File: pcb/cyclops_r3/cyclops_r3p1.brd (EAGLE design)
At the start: 69.8 x 53.3 mm, 55 parts, among them Q1 SUM11006, Q2 IRF510, U1 MCP4921, U2 317-N, U3 ADR03, U4 OP1177, U5 LM324N, U6 ZXTD45

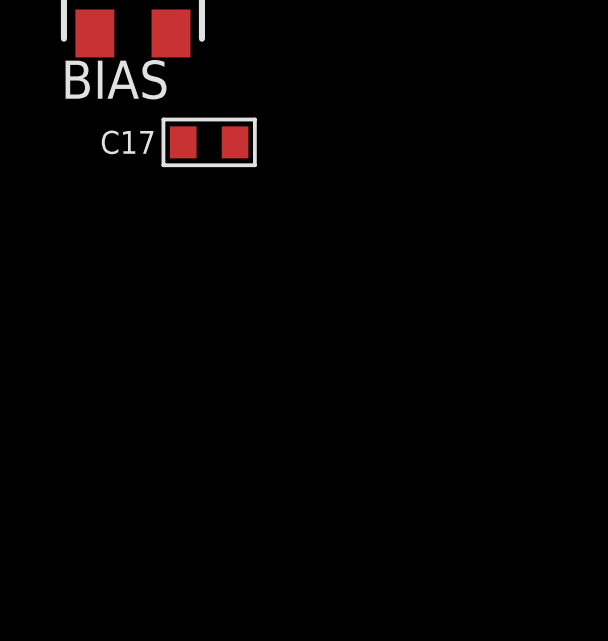
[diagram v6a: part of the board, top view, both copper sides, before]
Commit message: Added some test points to the the circuit and a design note.
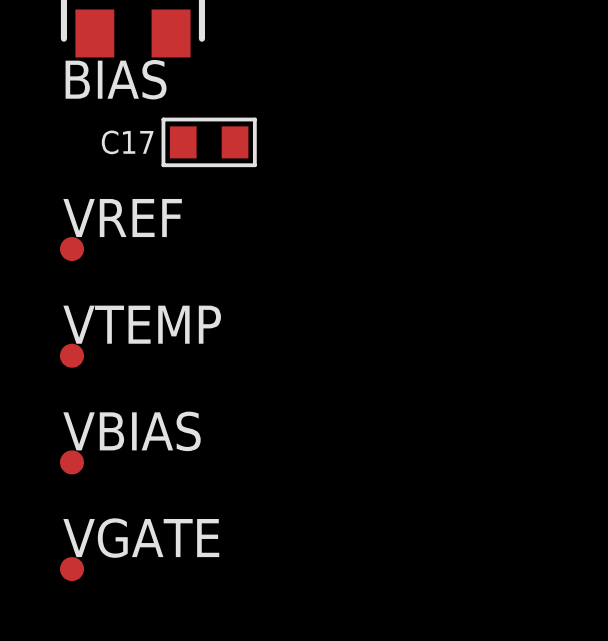
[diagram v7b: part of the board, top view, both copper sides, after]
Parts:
- added VBIAS, VGATE, VREF, VTEMP: TPTP08R, cyclops:TP08R
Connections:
- net REFA2X renamed VREF2X
- removed net REFA: C2.1, REF_ADJ.1, U1.6, U3.4, U5.12
- net N$13: now also VGATE.TP
- net N$4: now also VBIAS.TP
- net VREF: now also C2.1, REF_ADJ.1, U1.6, U3.4, U5.12, VREF.TP
- net VTEMP: now also VTEMP.TP
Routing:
- net VREF: track 40.7 -> 118.9 mm
- net REFA: track 78.2 -> 0.00 mm
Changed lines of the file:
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@@
 <element name="BIAS" library="cyclops" package="SM-42/43W" value="10k" x="-1.524" y="-13.716"/>
 <element name="C17" library="cyclops" package="0603" value=".1uF" x="1.016" y="-18.796"/>
+<element name="VREF" library="cyclops" package="TP08R" value="TPTP08R" x="-3.556" y="-22.352">
+<attribute name="TP_SIGNAL_NAME" value="" x="-3.556" y="-22.352" size="1.778" layer="27" display="off"/>
+</element>
+<element name="VTEMP" library="cyclops" package="TP08R" value="TPTP08R" x="-3.556" y="-25.908">
+<attribute name="TP_SIGNAL_NAME" value="" x="-3.556" y="-25.908" size="1.778" layer="27" display="off"/>
+</element>
+<element name="VBIAS" library="cyclops" package="TP08R" value="TPTP08R" x="-3.556" y="-29.464">
+<attribute name="TP_SIGNAL_NAME" value="" x="-3.556" y="-29.464" size="1.778" layer="27" display="off"/>
+</element>
+<element name="VGATE" library="cyclops" package="TP08R" value="TPTP08R" x="-3.556" y="-33.02">
+<attribute name="TP_SIGNAL_NAME" value="" x="-3.556" y="-33.02" size="1.778" layer="27" display="off"/>
+</element>
 </elements>
 <signals>
@@
 <wire x1="58.438" y1="39.116" x2="59.69" y2="39.116" width="0.254" layer="1"/>
 </signal>
-<signal name="REFA">
-<contactref element="U1" pad="6"/>
-<contactref element="C2" pad="1"/>
-<contactref element="U3" pad="4"/>
-<contactref element="REF_ADJ" pad="1"/>
-<wire x1="42.09" y1="28.9538" x2="42.09" y2="30.988" width="0.8128" layer="1"/>
-<wire x1="42.09" y1="30.988" x2="42.09" y2="31.168" width="0.8128" layer="1"/>
-<wire x1="42.09" y1="31.168" x2="42.164" y2="31.242" width="0.8128" layer="1"/>
-<wire x1="52.204078125" y1="31.242" x2="53.34" y2="32.377921875" width="0.8128" layer="1"/>
-<wire x1="53.34" y1="32.377921875" x2="53.34" y2="34.5186" width="0.8128" layer="1"/>
-<wire x1="53.34" y1="34.5186" x2="53.3654" y2="34.544" width="0.8128" layer="1"/>
-<wire x1="53.3654" y1="34.544" x2="53.3654" y2="34.5694" width="0.8128" layer="1"/>
-<wire x1="53.3654" y1="34.5694" x2="54.229" y2="35.433" width="0.6096" layer="1"/>
-<wire x1="54.229" y1="35.433" x2="56.328" y2="35.433" width="0.6096" layer="1"/>
-<wire x1="7.782" y1="49.022" x2="13.208" y2="49.022" width="0.4064" layer="1"/>
-<wire x1="13.208" y1="49.022" x2="13.97" y2="48.26" width="0.4064" layer="1"/>
-<wire x1="13.97" y1="48.26" x2="16.256" y2="48.26" width="0.4064" layer="1"/>
-<wire x1="16.256" y1="48.26" x2="17.018" y2="49.022" width="0.4064" layer="1"/>
-<wire x1="17.018" y1="49.022" x2="47.244" y2="49.022" width="0.4064" layer="1"/>
-<wire x1="47.244" y1="49.022" x2="49.276" y2="46.99" width="0.4064" layer="1"/>
-<wire x1="53.34" y1="35.56" x2="53.34" y2="34.5186" width="0.4064" layer="1"/>
-<wire x1="53.34" y1="34.5186" x2="53.34" y2="34.29" width="0.4064" layer="1"/>
-<wire x1="52.204078125" y1="31.242" x2="42.344" y2="31.242" width="0.8128" layer="1"/>
-<wire x1="42.344" y1="31.242" x2="42.09" y2="30.988" width="0.8128" layer="1"/>
-<wire x1="42.09" y1="28.9538" x2="42.5704" y2="28.4734" width="0.8128" layer="1"/>
-<wire x1="42.5704" y1="28.4734" x2="42.5704" y2="27.9654" width="0.8128" layer="1"/>
-<wire x1="49.276" y1="46.99" x2="49.276" y2="39.624" width="0.4064" layer="1"/>
-<wire x1="49.276" y1="39.624" x2="53.34" y2="35.56" width="0.4064" layer="1"/>
-<contactref element="U5" pad="12"/>
-<wire x1="42.09" y1="31.168" x2="28.448" y2="38.548" width="0" layer="19" extent="1-1"/>
-</signal>
 <signal name="DACA">
 <contactref element="U1" pad="8"/>
@@
 <wire x1="23.368" y1="39.116" x2="24.638" y2="39.116" width="0.4064" layer="1"/>
 <wire x1="24.638" y1="39.116" x2="24.638" y2="38.548" width="0.4064" layer="1"/>
+<contactref element="U1" pad="6"/>
+<contactref element="C2" pad="1"/>
+<contactref element="U3" pad="4"/>
+<contactref element="REF_ADJ" pad="1"/>
+<wire x1="42.09" y1="28.9538" x2="42.09" y2="30.988" width="0.8128" layer="1"/>
+<wire x1="42.09" y1="30.988" x2="42.09" y2="31.168" width="0.8128" layer="1"/>
+<wire x1="42.09" y1="31.168" x2="42.164" y2="31.242" width="0.8128" layer="1"/>
+<wire x1="52.204078125" y1="31.242" x2="53.34" y2="32.377921875" width="0.8128" layer="1"/>
+<wire x1="53.34" y1="32.377921875" x2="53.34" y2="34.5186" width="0.8128" layer="1"/>
+<wire x1="53.34" y1="34.5186" x2="53.3654" y2="34.544" width="0.8128" layer="1"/>
+<wire x1="53.3654" y1="34.544" x2="53.3654" y2="34.5694" width="0.8128" layer="1"/>
+<wire x1="53.3654" y1="34.5694" x2="54.229" y2="35.433" width="0.6096" layer="1"/>
+<wire x1="54.229" y1="35.433" x2="56.328" y2="35.433" width="0.6096" layer="1"/>
+<wire x1="7.782" y1="49.022" x2="13.208" y2="49.022" width="0.4064" layer="1"/>
+<wire x1="13.208" y1="49.022" x2="13.97" y2="48.26" width="0.4064" layer="1"/>
+<wire x1="13.97" y1="48.26" x2="16.256" y2="48.26" width="0.4064" layer="1"/>
+<wire x1="16.256" y1="48.26" x2="17.018" y2="49.022" width="0.4064" layer="1"/>
+<wire x1="17.018" y1="49.022" x2="47.244" y2="49.022" width="0.4064" layer="1"/>
+<wire x1="47.244" y1="49.022" x2="49.276" y2="46.99" width="0.4064" layer="1"/>
+<wire x1="53.34" y1="35.56" x2="53.34" y2="34.5186" width="0.4064" layer="1"/>
+<wire x1="53.34" y1="34.5186" x2="53.34" y2="34.29" width="0.4064" layer="1"/>
+<wire x1="52.204078125" y1="31.242" x2="42.344" y2="31.242" width="0.8128" layer="1"/>
+<wire x1="42.344" y1="31.242" x2="42.09" y2="30.988" width="0.8128" layer="1"/>
+<wire x1="42.09" y1="28.9538" x2="42.5704" y2="28.4734" width="0.8128" layer="1"/>
+<wire x1="42.5704" y1="28.4734" x2="42.5704" y2="27.9654" width="0.8128" layer="1"/>
+<wire x1="49.276" y1="46.99" x2="49.276" y2="39.624" width="0.4064" layer="1"/>
+<wire x1="49.276" y1="39.624" x2="53.34" y2="35.56" width="0.4064" layer="1"/>
+<contactref element="U5" pad="12"/>
+<contactref element="VREF" pad="TP"/>
+<wire x1="24.638" y1="38.548" x2="28.448" y2="38.548" width="0" layer="19" extent="1-1"/>
+<wire x1="13.97" y1="48.26" x2="13.148" y2="39.056" width="0" layer="19" extent="1-1"/>
+<wire x1="-3.556" y1="-22.352" x2="3.556" y2="14.986" width="0" layer="19" extent="1-1"/>
 </signal>
 <signal name="VAUX">
@@
 <wire x1="36.449" y1="26.289" x2="37.084" y2="26.924" width="0.4064" layer="16"/>
 <wire x1="37.084" y1="26.924" x2="45.974" y2="26.924" width="0.4064" layer="16"/>
+<contactref element="VTEMP" pad="TP"/>
+<wire x1="3.556" y1="12.446" x2="-3.556" y2="-25.908" width="0" layer="19" extent="1-1"/>
 </signal>
 <signal name="VCTL">
@@
 <wire x1="12.7" y1="21.4884" x2="11.7983" y2="21.4884" width="0.6096" layer="16"/>
 <wire x1="11.7983" y1="21.4884" x2="10.16" y2="23.1267" width="0.6096" layer="16"/>
-<wire x1="10.16" y1="23.1267" x2="8.382" y2="25.5524" width="0" layer="19" extent="16-16"/>
-</signal>
-<signal name="REFA2X">
+<contactref element="VGATE" pad="TP"/>
+<wire x1="11.7983" y1="21.4884" x2="-3.556" y2="-33.02" width="0" layer="19" extent="1-16"/>
+<wire x1="8.382" y1="25.5524" x2="10.16" y2="23.1267" width="0" layer="19" extent="16-16"/>
+</signal>
+<signal name="VREF2X">
 <contactref element="S3" pad="1"/>
 <contactref element="R15" pad="2"/>
@@
 <wire x1="29.972" y1="41.402" x2="30.48" y2="41.91" width="0.4064" layer="16"/>
 <wire x1="30.48" y1="41.91" x2="30.988" y2="42.418" width="0.4064" layer="1"/>
+<contactref element="VBIAS" pad="TP"/>
 <wire x1="30.988" y1="42.418" x2="30.988" y2="43.748" width="0" layer="19" extent="1-1"/>
 <wire x1="-1.524" y1="-12.266" x2="12.2604" y2="26.3144" width="0" layer="19" extent="1-16"/>
+<wire x1="-3.556" y1="-29.464" x2="-1.524" y2="-12.266" width="0" layer="19" extent="1-1"/>
 </signal>
 <signal name="AGND">
@@
 </signal>
 </signals>
-<errors>
-</errors>
 </board>
 </drawing>

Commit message: Forgot to save board in my last commit.
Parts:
- moved C17 73.3 mm to (47.2, 38.1), turned to 90 degrees
- moved BIAS 68.8 mm to (43.7, 38.1), turned to 90 degrees
- moved C16 66.1 mm to (37.1, 47.2)
- moved R15 62.0 mm to (33.5, 46.7)
- moved R14 56.2 mm to (38.1, 38.1)
- moved R13 52.0 mm to (34.0, 38.1), turned to 180 degrees
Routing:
- net VREF: track 118.9 -> 113.5 mm
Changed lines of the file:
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@@
 <layer number="20" name="Dimension" color="15" fill="1" visible="yes" active="yes"/>
 <layer number="21" name="tPlace" color="7" fill="1" visible="yes" active="yes"/>
-<layer number="22" name="bPlace" color="7" fill="1" visible="yes" active="yes"/>
+<layer number="22" name="bPlace" color="7" fill="1" visible="no" active="yes"/>
 <layer number="23" name="tOrigins" color="15" fill="1" visible="yes" active="yes"/>
 <layer number="24" name="bOrigins" color="15" fill="1" visible="yes" active="yes"/>
-<layer number="25" name="tNames" color="7" fill="1" visible="yes" active="yes"/>
-<layer number="26" name="bNames" color="7" fill="1" visible="yes" active="yes"/>
-<layer number="27" name="tValues" color="7" fill="1" visible="yes" active="yes"/>
-<layer number="28" name="bValues" color="7" fill="1" visible="yes" active="yes"/>
-<layer number="29" name="tStop" color="7" fill="3" visible="yes" active="yes"/>
+<layer number="25" name="tNames" color="7" fill="1" visible="no" active="yes"/>
+<layer number="26" name="bNames" color="7" fill="1" visible="no" active="yes"/>
+<layer number="27" name="tValues" color="7" fill="1" visible="no" active="yes"/>
+<layer number="28" name="bValues" color="7" fill="1" visible="no" active="yes"/>
+<layer number="29" name="tStop" color="7" fill="3" visible="no" active="yes"/>
 <layer number="30" name="bStop" color="7" fill="6" visible="no" active="yes"/>
 <layer number="31" name="tCream" color="7" fill="4" visible="no" active="yes"/>
@@
 <attribute name="NAME" x="9.652" y="0.381" size="0.889" layer="25" font="vector" ratio="18"/>
 </element>
-<element name="R13" library="cyclops" package="0603" value="1k" x="1.016" y="-2.032">
-<attribute name="MN" value="Panasonic" x="1.016" y="-2.032" size="1.778" layer="27" display="off"/>
-<attribute name="DK" value="PxxxxHTR-ND" x="1.016" y="-2.032" size="1.778" layer="27" display="off"/>
-<attribute name="MPN" value="ERJ-3EKFxxxxV" x="1.016" y="-2.032" size="1.778" layer="27" display="off"/>
-</element>
-<element name="R14" library="cyclops" package="0603" value="1k" x="1.016" y="-4.064">
-<attribute name="MN" value="Panasonic" x="1.016" y="-4.064" size="1.778" layer="27" display="off"/>
-<attribute name="DK" value="PxxxxHTR-ND" x="1.016" y="-4.064" size="1.778" layer="27" display="off"/>
-<attribute name="MPN" value="ERJ-3EKFxxxxV" x="1.016" y="-4.064" size="1.778" layer="27" display="off"/>
-</element>
-<element name="R15" library="cyclops" package="0603" value="1k" x="1.016" y="-6.096">
-<attribute name="MN" value="Panasonic" x="1.016" y="-6.096" size="1.778" layer="27" display="off"/>
-<attribute name="DK" value="PxxxxHTR-ND" x="1.016" y="-6.096" size="1.778" layer="27" display="off"/>
-<attribute name="MPN" value="ERJ-3EKFxxxxV" x="1.016" y="-6.096" size="1.778" layer="27" display="off"/>
-</element>
-<element name="C16" library="cyclops" package="0603" value=".1uF" x="1.016" y="-8.128"/>
-<element name="BIAS" library="cyclops" package="SM-42/43W" value="10k" x="-1.524" y="-13.716"/>
-<element name="C17" library="cyclops" package="0603" value=".1uF" x="1.016" y="-18.796"/>
+<element name="R13" library="cyclops" package="0603" value="1k" x="34.036" y="38.1" rot="R180">
+<attribute name="MN" value="Panasonic" x="34.036" y="38.1" size="1.778" layer="27" rot="R180" display="off"/>
+<attribute name="DK" value="PxxxxHTR-ND" x="34.036" y="38.1" size="1.778" layer="27" rot="R180" display="off"/>
+<attribute name="MPN" value="ERJ-3EKFxxxxV" x="34.036" y="38.1" size="1.778" layer="27" rot="R180" display="off"/>
+</element>
+<element name="R14" library="cyclops" package="0603" value="1k" x="38.1" y="38.1">
+<attribute name="MN" value="Panasonic" x="38.1" y="38.1" size="1.778" layer="27" display="off"/>
+<attribute name="DK" value="PxxxxHTR-ND" x="38.1" y="38.1" size="1.778" layer="27" display="off"/>
+<attribute name="MPN" value="ERJ-3EKFxxxxV" x="38.1" y="38.1" size="1.778" layer="27" display="off"/>
+</element>
+<element name="R15" library="cyclops" package="0603" value="1k" x="33.528" y="46.736">
+<attribute name="MN" value="Panasonic" x="33.528" y="46.736" size="1.778" layer="27" display="off"/>
+<attribute name="DK" value="PxxxxHTR-ND" x="33.528" y="46.736" size="1.778" layer="27" display="off"/>
+<attribute name="MPN" value="ERJ-3EKFxxxxV" x="33.528" y="46.736" size="1.778" layer="27" display="off"/>
+</element>
+<element name="C16" library="cyclops" package="0603" value=".1uF" x="37.084" y="47.244"/>
+<element name="BIAS" library="cyclops" package="SM-42/43W" value="10k" x="43.688" y="38.1" rot="R90"/>
+<element name="C17" library="cyclops" package="0603" value=".1uF" x="47.244" y="38.1" rot="R90"/>
 <element name="VREF" library="cyclops" package="TP08R" value="TPTP08R" x="-3.556" y="-22.352">
 <attribute name="TP_SIGNAL_NAME" value="" x="-3.556" y="-22.352" size="1.778" layer="27" display="off"/>
@@
 <contactref element="BIAS" pad="1"/>
 <contactref element="C17" pad="1"/>
-<wire x1="46.7614" y1="20.574" x2="46.736" y2="20.574" width="0" layer="19" extent="1-1"/>
+<wire x1="45.138" y1="36.83" x2="47.244" y2="37.2364" width="0" layer="19" extent="1-1"/>
+<wire x1="39.624" y1="43.964" x2="45.138" y2="36.83" width="0" layer="19" extent="1-1"/>
+<wire x1="46.736" y1="20.574" x2="46.7614" y2="20.574" width="0" layer="19" extent="1-1"/>
 <wire x1="24.257" y1="27.7495" x2="24.257" y2="27.686" width="0" layer="19" extent="16-16"/>
 <wire x1="33.9852" y1="27.7495" x2="27.305" y2="27.686" width="0" layer="19" extent="16-16"/>
 <wire x1="12.362" y1="25.466" x2="20.193" y2="25.654" width="0" layer="19" extent="16-16"/>
-<wire x1="-2.794" y1="-15.166" x2="3.556" y2="7.366" width="0" layer="19" extent="1-1"/>
-<wire x1="0.1524" y1="-18.796" x2="-2.794" y2="-15.166" width="0" layer="19" extent="1-1"/>
 </signal>
 <signal name="N$72">
@@
 <wire x1="53.3654" y1="34.5694" x2="54.229" y2="35.433" width="0.6096" layer="1"/>
 <wire x1="54.229" y1="35.433" x2="56.328" y2="35.433" width="0.6096" layer="1"/>
-<wire x1="7.782" y1="49.022" x2="13.208" y2="49.022" width="0.4064" layer="1"/>
 <wire x1="13.208" y1="49.022" x2="13.97" y2="48.26" width="0.4064" layer="1"/>
 <wire x1="13.97" y1="48.26" x2="16.256" y2="48.26" width="0.4064" layer="1"/>
@@
 <wire x1="42.852" y1="34.29" x2="44.3484" y2="34.29" width="0.8128" layer="1"/>
 </signal>
-<signal name="GND">
+<signal name="GND" airwireshidden="yes">
 <contactref element="C4" pad="2"/>
 <contactref element="C3" pad="2"/>
@@
 <contactref element="R13" pad="2"/>
 <contactref element="C16" pad="2"/>
-<wire x1="1.8796" y1="-2.032" x2="1.8796" y2="-8.128" width="0" layer="19" extent="1-1"/>
-<wire x1="3.556" y1="4.826" x2="1.8796" y2="-2.032" width="0" layer="19" extent="1-1"/>
+<wire x1="36.576" y1="45.212" x2="37.9476" y2="47.244" width="0" layer="19" extent="1-1"/>
+<wire x1="33.1724" y1="38.1" x2="27.178" y2="38.548" width="0" layer="19" extent="1-1"/>
 </signal>
 <signal name="VIN">
@@
 <contactref element="R15" pad="2"/>
 <contactref element="C16" pad="1"/>
-<wire x1="1.8796" y1="-6.096" x2="7.66" y2="49.144" width="0" layer="19" extent="1-1"/>
-<wire x1="0.1524" y1="-8.128" x2="1.8796" y2="-6.096" width="0" layer="19" extent="1-1"/>
+<wire x1="34.3916" y1="46.736" x2="36.2204" y2="47.244" width="0" layer="19" extent="1-1"/>
+<wire x1="7.66" y1="49.144" x2="34.3916" y2="46.736" width="0" layer="19" extent="1-1"/>
 </signal>
 <signal name="VREFA2X">
@@
 <contactref element="R13" pad="1"/>
 <contactref element="R15" pad="1"/>
-<wire x1="0.1524" y1="-2.032" x2="30.988" y2="38.548" width="0" layer="19" extent="1-1"/>
-<wire x1="0.1524" y1="-4.064" x2="0.1524" y2="-2.032" width="0" layer="19" extent="1-1"/>
-<wire x1="0.1524" y1="-6.096" x2="0.1524" y2="-4.064" width="0" layer="19" extent="1-1"/>
+<wire x1="30.988" y1="38.548" x2="32.6644" y2="46.736" width="0" layer="19" extent="1-1"/>
+<wire x1="34.8996" y1="38.1" x2="30.988" y2="38.548" width="0" layer="19" extent="1-1"/>
+<wire x1="37.2364" y1="38.1" x2="34.8996" y2="38.1" width="0" layer="19" extent="1-1"/>
 </signal>
 <signal name="N$8">
 <contactref element="U5" pad="13"/>
 <contactref element="R14" pad="2"/>
-<wire x1="1.8796" y1="-4.064" x2="29.718" y2="38.548" width="0" layer="19" extent="1-1"/>
+<wire x1="29.718" y1="38.548" x2="38.9636" y2="38.1" width="0" layer="19" extent="1-1"/>
 </signal>
 <signal name="N$4">
@@
 <wire x1="30.48" y1="41.91" x2="30.988" y2="42.418" width="0.4064" layer="1"/>
 <contactref element="VBIAS" pad="TP"/>
-<wire x1="30.988" y1="42.418" x2="30.988" y2="43.748" width="0" layer="19" extent="1-1"/>
-<wire x1="-1.524" y1="-12.266" x2="12.2604" y2="26.3144" width="0" layer="19" extent="1-16"/>
-<wire x1="-3.556" y1="-29.464" x2="-1.524" y2="-12.266" width="0" layer="19" extent="1-1"/>
+<wire x1="30.988" y1="42.418" x2="42.238" y2="38.1" width="0" layer="19" extent="1-1"/>
+<wire x1="30.988" y1="43.748" x2="30.988" y2="42.418" width="0" layer="19" extent="1-1"/>
+<wire x1="-3.556" y1="-29.464" x2="12.2604" y2="26.3144" width="0" layer="19" extent="1-16"/>
 </signal>
 <signal name="AGND">
 <contactref element="BIAS" pad="3"/>
 <contactref element="C17" pad="2"/>
-<wire x1="-0.254" y1="-15.166" x2="1.8796" y2="-18.796" width="0" layer="19" extent="1-1"/>
+<wire x1="45.138" y1="39.37" x2="47.244" y2="38.9636" width="0" layer="19" extent="1-1"/>
 </signal>
 </signals>
